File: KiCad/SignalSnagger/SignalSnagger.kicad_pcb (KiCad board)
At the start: 4 copper layers, 133.4 x 44.3 mm, 179 parts, among them J102 Left, J104 Right, J105 36-5005-ND, J106 36-5006-ND, J107 36-5006-ND, J108 36-5005-ND, J109 36-5006-ND, J110 36-5006-ND, J203 Conn_01x02, J204 Conn_01x02, J301 35RASMT2BHSNTRX, J302 36-5005-ND, J303 36-5005-ND, J304 36-5006-ND, P201 ISP/PDI, Q101 MMBT2222A, Q102 MMBT2222A, Q103 MMBT2222A, Q104 MMBT2222A, Q105 MMBT2222A, Q201 BSS84W-7-F, Q202 BSS138W-7-F, SW201 SW_SPST, SW202 SW_SPST, SW203 PEC12R-4225F-S0024, T101 Transformer_1P_SS, U102 QS3253QG8, U103 REF4132B33, U104 DG9422E, U105 DG9422E, U201 AVR128DA48, U202 SI5351, U203 LP2985-5.0, U204 LP2985-3.3, U205 EA_DOGS104W-A, U206 LP2985-5.0, U207 MAX1683EUK, U302 TS912IDT, U303 TS912IDT, U304 LM386, X201 ECS-327TXO-30-TR, X202 25 MHz

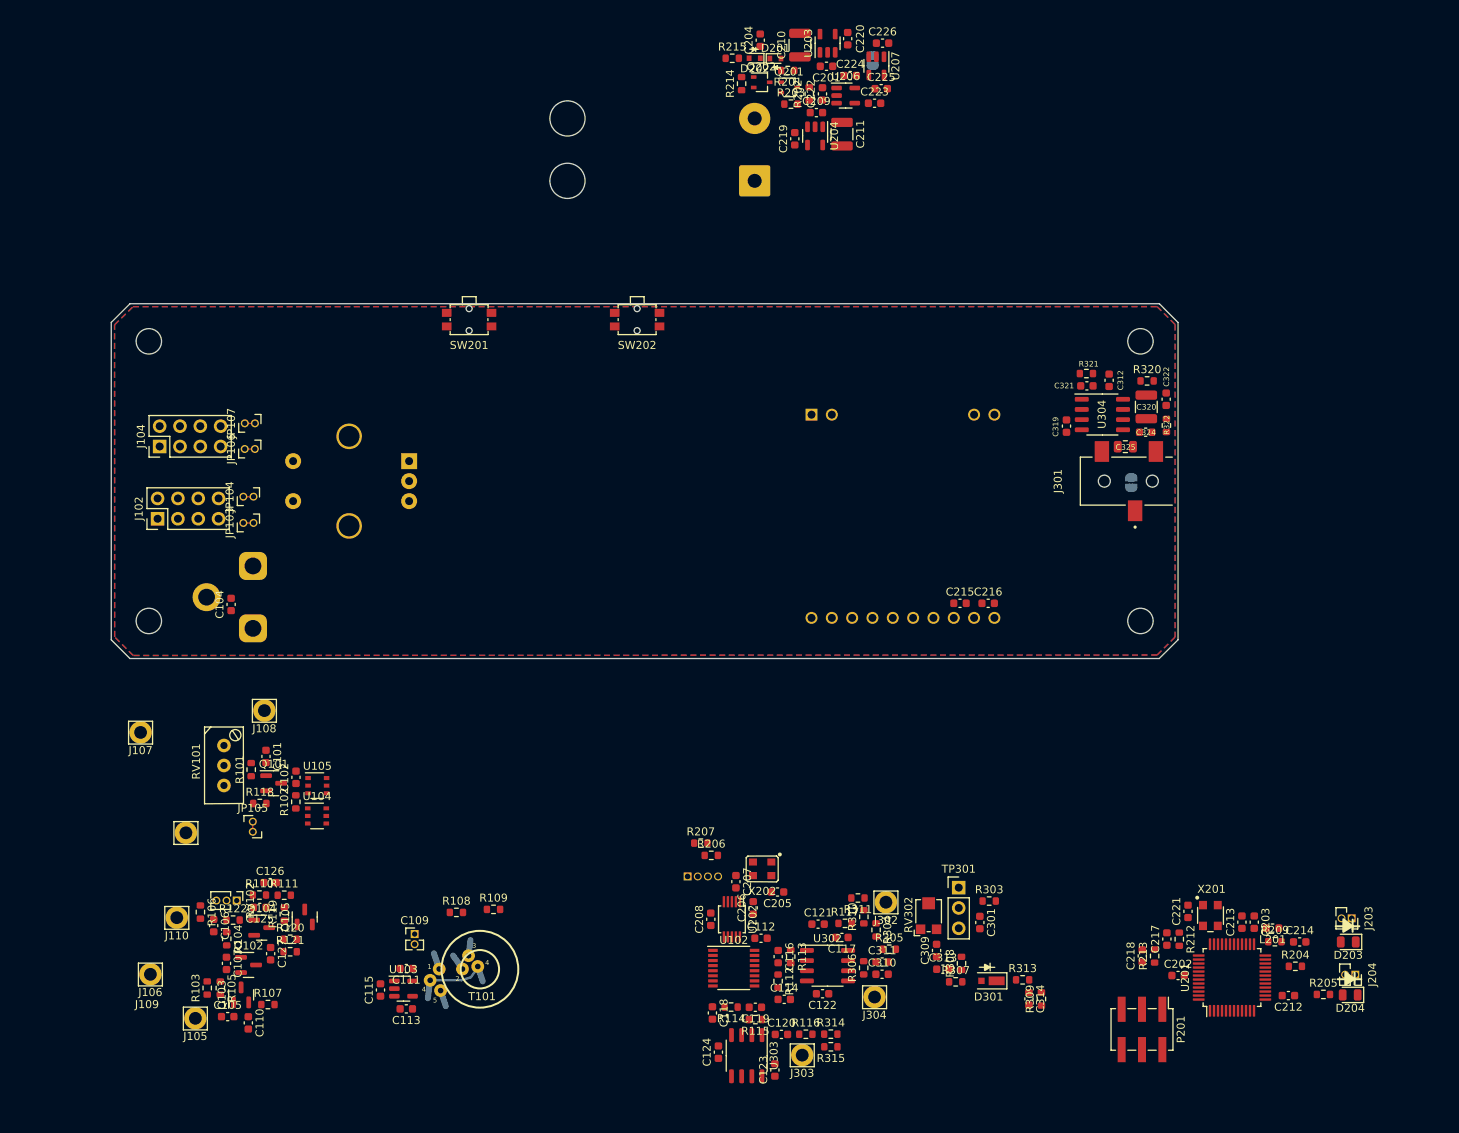
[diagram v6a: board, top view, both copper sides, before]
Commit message: Ver 0.305
PCB Layout Changes
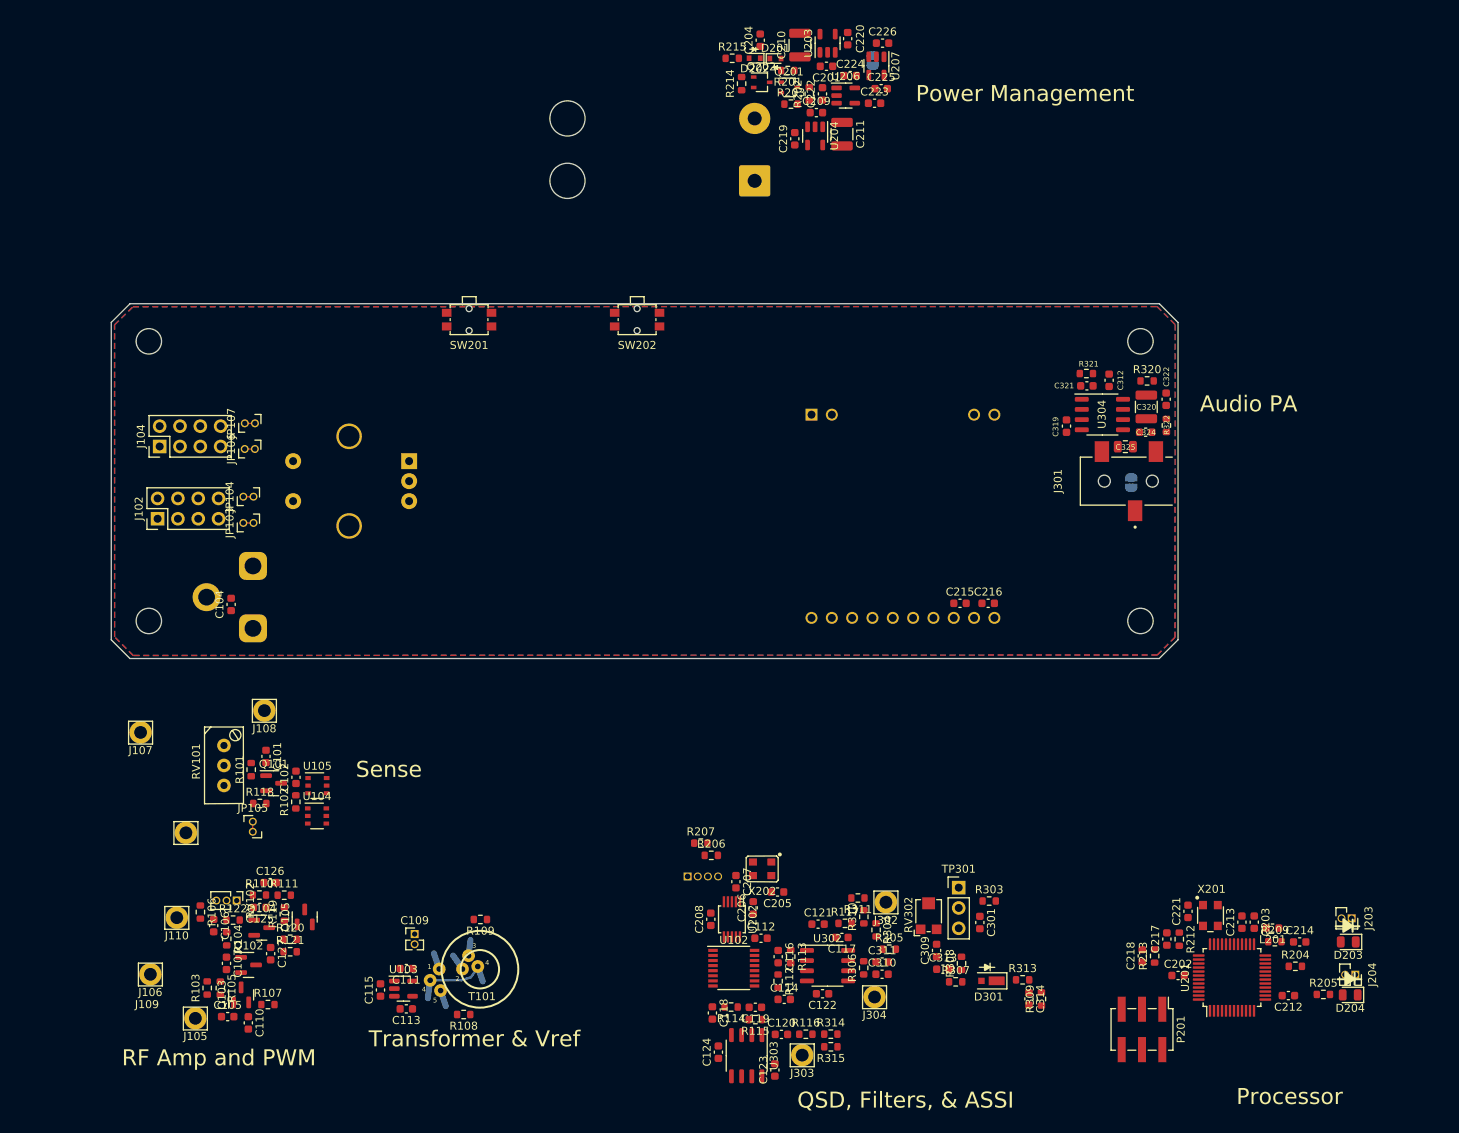
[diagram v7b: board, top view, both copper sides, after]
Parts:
- moved R108 12.8 mm to (121.3, 162.9), turned to 180 degrees
- moved R109 2.07 mm to (123.4, 151.0), turned to 180 degrees
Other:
- board text added: "Audio PA"
- board text added: "Power Management"
- board text added: "Processor"
- board text added: "QSD, Filters, & ASSI"
- board text added: "RF Amp and PWM"
- board text added: "Sense"
- board text added: "Transformer & Vref"
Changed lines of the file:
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@@
   )
   (footprint "Resistor_SMD:R_0603_1608Metric" (layer "F.Cu")
-    (at 125.05 149.715)
+    (at 123.41 150.98 180)
     (descr "Resistor SMD 0603 (1608 Metric), square (rectangular) end terminal, IPC_7351 nominal, (Body size source: IPC-SM-782 page 72, https://www.pcb-3d.com/wordpress/wp-content/uploads/ipc-sm-782a_amendment_1_and_2.pdf), generated with kicad-footprint-generator")
     (tags "resistor")
@@
     (fp_line (start -0.8 -0.4125) (end 0.8 -0.4125) (layer "F.Fab") (width 0.1))
     (fp_line (start 0.8 -0.4125) (end 0.8 0.4125) (layer "F.Fab") (width 0.1))
-    (pad "1" smd roundrect (at -0.825 0) (size 0.8 0.95) (layers "F.Cu" "F.Paste" "F.Mask") (roundrect_rratio 0.25)
+    (pad "1" smd roundrect (at -0.825 0 180) (size 0.8 0.95) (layers "F.Cu" "F.Paste" "F.Mask") (roundrect_rratio 0.25)
       (net 90 "Net-(R109-Pad1)") (pintype "passive"))
-    (pad "2" smd roundrect (at 0.825 0) (size 0.8 0.95) (layers "F.Cu" "F.Paste" "F.Mask") (roundrect_rratio 0.25)
+    (pad "2" smd roundrect (at 0.825 0 180) (size 0.8 0.95) (layers "F.Cu" "F.Paste" "F.Mask") (roundrect_rratio 0.25)
       (net 91 "Net-(R109-Pad2)") (pintype "passive"))
     (model "${KICAD6_3DMODEL_DIR}/Resistor_SMD.3dshapes/R_0603_1608Metric.wrl"
@@
   )
   (footprint "Resistor_SMD:R_0603_1608Metric" (layer "F.Cu")
-    (at 120.41 150.095)
+    (at 121.32 162.86 180)
     (descr "Resistor SMD 0603 (1608 Metric), square (rectangular) end terminal, IPC_7351 nominal, (Body size source: IPC-SM-782 page 72, https://www.pcb-3d.com/wordpress/wp-content/uploads/ipc-sm-782a_amendment_1_and_2.pdf), generated with kicad-footprint-generator")
     (tags "resistor")
@@
     (fp_line (start 0.8 0.4125) (end -0.8 0.4125) (layer "F.Fab") (width 0.1))
     (fp_line (start -0.8 0.4125) (end -0.8 -0.4125) (layer "F.Fab") (width 0.1))
-    (pad "1" smd roundrect (at -0.825 0) (size 0.8 0.95) (layers "F.Cu" "F.Paste" "F.Mask") (roundrect_rratio 0.25)
+    (pad "1" smd roundrect (at -0.825 0 180) (size 0.8 0.95) (layers "F.Cu" "F.Paste" "F.Mask") (roundrect_rratio 0.25)
       (net 88 "Net-(R108-Pad1)") (pintype "passive"))
-    (pad "2" smd roundrect (at 0.825 0) (size 0.8 0.95) (layers "F.Cu" "F.Paste" "F.Mask") (roundrect_rratio 0.25)
+    (pad "2" smd roundrect (at 0.825 0 180) (size 0.8 0.95) (layers "F.Cu" "F.Paste" "F.Mask") (roundrect_rratio 0.25)
       (net 89 "Net-(R108-Pad2)") (pintype "passive"))
     (model "${KICAD6_3DMODEL_DIR}/Resistor_SMD.3dshapes/R_0603_1608Metric.wrl"
@@
   (gr_line locked (start 210.615 76.35125) (end 210.615 116.021) (layer "Edge.Cuts") (width 0.1))
   (gr_line locked (start 79.61 74.012) (end 208.283 74.012) (layer "Edge.Cuts") (width 0.1))
+  (gr_text "Transformer & Vref" (at 122.67 165.91) (layer "F.SilkS")
+    (effects (font (size 2 2) (thickness 0.15)))
+  )
+  (gr_text "Audio PA" (at 219.44 86.54) (layer "F.SilkS")
+    (effects (font (size 2 2) (thickness 0.15)))
+  )
+  (gr_text "Power Management" (at 191.5 47.75) (layer "F.SilkS")
+    (effects (font (size 2 2) (thickness 0.15)))
+  )
+  (gr_text "QSD, Filters, & ASSI" (at 176.56 173.57) (layer "F.SilkS")
+    (effects (font (size 2 2) (thickness 0.15)))
+  )
+  (gr_text "RF Amp and PWM" (at 90.73 168.28) (layer "F.SilkS")
+    (effects (font (size 2 2) (thickness 0.15)))
+  )
+  (gr_text "Processor" (at 224.56 173.12) (layer "F.SilkS")
+    (effects (font (size 2 2) (thickness 0.15)))
+  )
+  (gr_text "Sense" (at 111.97 132.23) (layer "F.SilkS")
+    (effects (font (size 2 2) (thickness 0.15)))
+  )
   (zone locked (net 70) (net_name "Net-(J102-Pad8)") (layer "F.Cu") (hatch edge 0.508)
     (connect_pads (clearance 0.508))

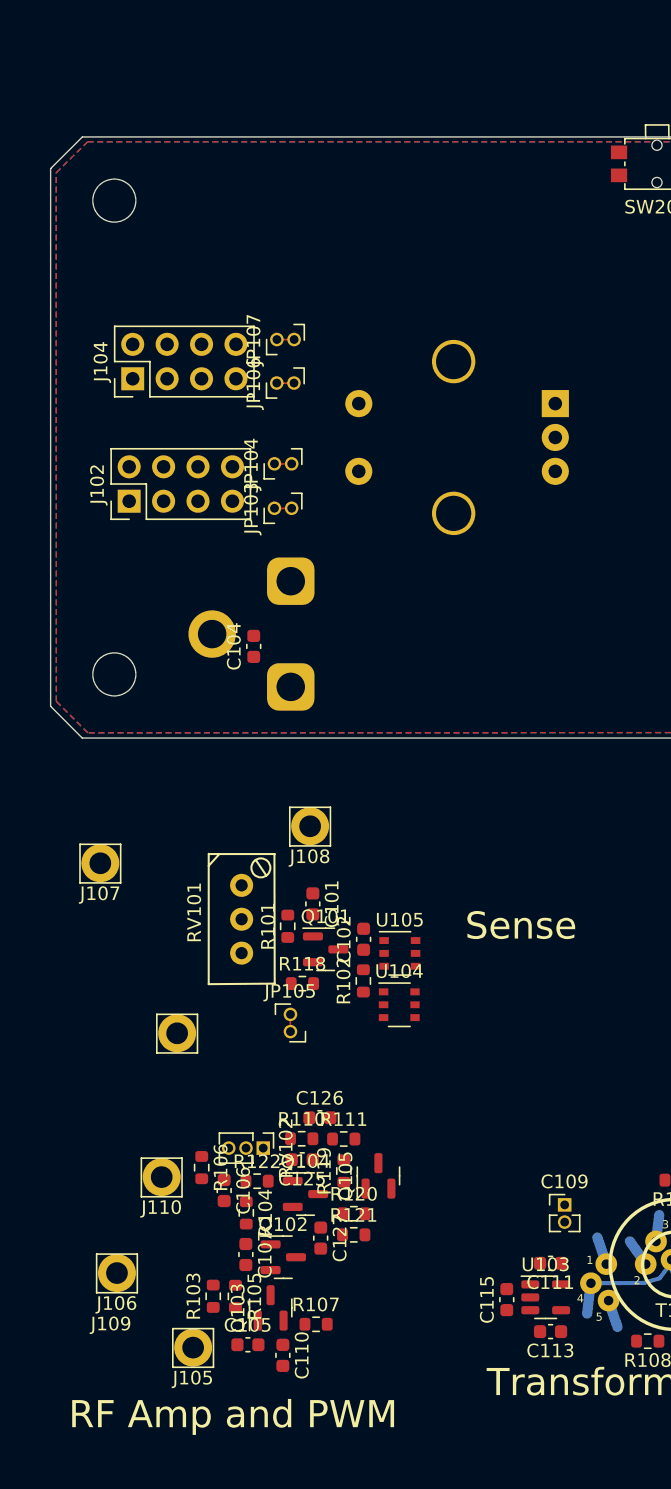
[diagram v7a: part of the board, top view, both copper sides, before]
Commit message: PCB Updates
Ver 0.306
Brought in Jerry's layout of RF components.
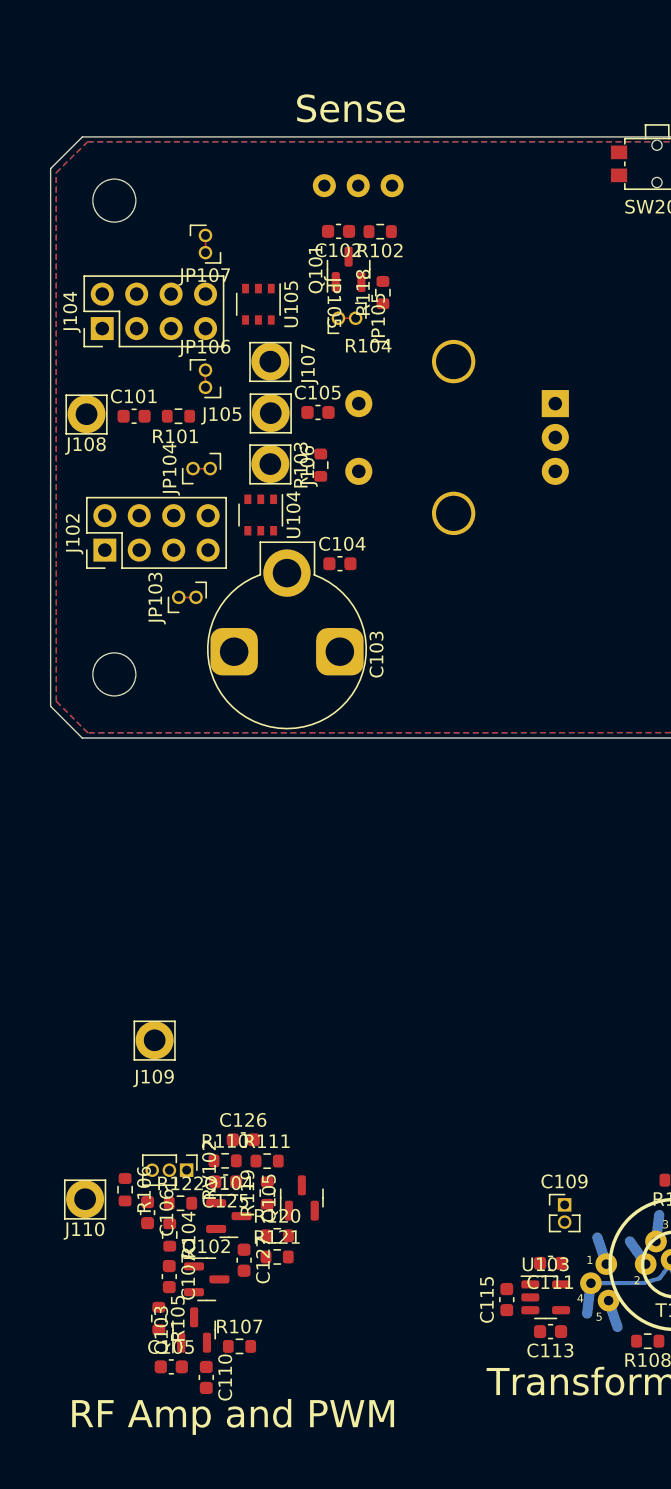
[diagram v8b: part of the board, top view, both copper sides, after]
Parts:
- added C105: 10nF, Capacitor_SMD:C_0603_1608Metric, F.Cu at (97.0, 94.3)
- C103: moved to F.Cu
- RV101: moved to B.Cu
- moved J105 69.2 mm to (93.5, 94.4)
- moved R103 61.8 mm to (97.2, 98.2)
- moved J106 60.7 mm to (93.5, 98.2)
- moved R102 55.3 mm to (101.6, 81.0), turned to 180 degrees
- moved RV101 54.8 mm to (100.0, 77.6), turned to -90 degrees
- moved C102 52.3 mm to (98.5, 81.0), turned to 180 degrees
- moved JP105 51.6 mm to (99.8, 87.4), turned to -90 degrees
- moved R118 51.3 mm to (101.8, 85.5), turned to 90 degrees
- moved Q101 50.2 mm to (99.2, 83.8), turned to 90 degrees
- moved U105 49.0 mm to (92.6, 86.4), turned to -90 degrees
- moved J107 39.1 mm to (93.5, 90.6)
- moved R101 38.5 mm to (86.7, 94.6), turned to 180 degrees
- moved C101 38.3 mm to (83.4, 94.6), turned to 0 degrees
- moved U104 37.5 mm to (92.8, 101.9), turned to -90 degrees
- moved J108 34.6 mm to (79.9, 94.5)
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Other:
- board text added: "JP105"
- board text added: "R104"
